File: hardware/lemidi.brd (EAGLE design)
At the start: 76 x 40 mm, 67 parts, among them Q1 IRLML6246, Q2 IRLML6246, Q3 IRLML6246, Q4 IRLML6246, U1 SPX5205 3v3, X1 optional 5V input, X3 debug, Y2 12MHz 0.25%, Y3 8MHz

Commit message: 2nd cleanup
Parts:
- moved U$7 0.72 mm to (72.2, 3.75)
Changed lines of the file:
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@@
 <text x="1.8" y="9.4" size="1.016" layer="1" font="vector" ratio="15" rot="R90">1</text>
 <text x="1.8" y="11.2" size="1.016" layer="16" font="vector" ratio="15" rot="R90">2</text>
-<text x="72.7" y="1.13" size="0.8128" layer="109" font="vector" ratio="15" rot="MR90">github.com/rodan/lemidi</text>
-<text x="74.13" y="1.15" size="0.8128" layer="109" font="vector" ratio="15" rot="MR90">Petre Rodan 201901 rev1</text>
+<text x="71.7" y="7.53" size="0.8128" layer="109" font="vector" ratio="15" rot="MR90">github.com/rodan/lemidi</text>
+<text x="73.13" y="7.55" size="0.8128" layer="109" font="vector" ratio="15" rot="MR90">Petre Rodan 201901 rev1</text>
 <text x="2.23" y="36.83" size="0.8128" layer="109" font="vector" ratio="15" rot="MR270">debug</text>
 <wire x1="1.35" y1="9.35" x2="1.35" y2="12.15" width="1.6764" layer="41"/>
@@
 <element name="C4" library="rcl" package="C0805" value="1uF" x="29.75" y="8.53" rot="R90"/>
 <element name="C6" library="rcl" package="C0805" value="100nF" x="26.55" y="5.43"/>
-<element name="U$7" library="SparkFun" package="OSHW-LOGO-M" value="OSHW-LOGOM" x="71.81" y="4.35" rot="MR90"/>
+<element name="U$7" library="SparkFun" package="OSHW-LOGO-M" value="OSHW-LOGOM" x="72.21" y="3.75" rot="MR90"/>
 <element name="U$1" library="TI_MSP430_v16" package="PT48" value="MSP430F5510" x="28.8" y="28.8"/>
 <element name="C10" library="rcl" package="C0805" value="470nF" x="20.8" y="25" rot="R180"/>

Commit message: 3rd cleanup
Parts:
- removed X1: optional 5V input, Simplex-Connectors:0530480210
- added JP1: external 5v, SparkFun-Connectors:1X02
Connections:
- net 5V_EXT: now also JP1.1; no longer X1.2
- net GND: now also JP1.2; no longer X1.1
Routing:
- net 5V_EXT: track 9.18 -> 8.50 mm
- net GND: vias 35 -> 37
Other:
- board text added: "3V3"
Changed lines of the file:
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@@
 <layer number="97" name="Info" color="7" fill="1" visible="no" active="no"/>
 <layer number="98" name="Guide" color="6" fill="1" visible="no" active="no"/>
+<layer number="99" name="SpiceOrder" color="7" fill="1" visible="no" active="no"/>
 <layer number="100" name="Muster" color="7" fill="1" visible="no" active="no"/>
 <layer number="101" name="Patch_Top" color="12" fill="4" visible="no" active="yes"/>
@@
 <hole x="3.1" y="3.1" drill="3.2"/>
 <rectangle x1="19.7" y1="6.5" x2="21.2" y2="8" layer="30"/>
-<text x="34.73" y="0.97" size="0.8128" layer="109" font="vector" ratio="15" rot="MR0">ext 5V</text>
+<text x="30.47" y="0.77" size="0.8128" layer="108" font="vector" ratio="15">ext 5V</text>
 <text x="1.8" y="9.4" size="1.016" layer="1" font="vector" ratio="15" rot="R90">1</text>
 <text x="1.8" y="11.2" size="1.016" layer="16" font="vector" ratio="15" rot="R90">2</text>
@@
 <wire x1="17.6" y1="29.8" x2="18" y2="29.8" width="0.254" layer="109"/>
 <wire x1="18" y1="29.8" x2="18.8" y2="30.6" width="0.254" layer="109"/>
+<text x="23.27" y="12.57" size="0.8128" layer="108" font="vector" ratio="15">3V3</text>
 </plain>
 <attributes>
@@
 <element name="C3" library="rcl" package="C0805" value="10uF" x="26.55" y="3.33"/>
 <element name="X3" library="Simplex-Connectors" package="0530480610" value="debug" x="4.6" y="38.4" rot="R270"/>
-<element name="X1" library="Simplex-Connectors" package="0530480210" value="optional 5V input" x="32.2" y="4.2"/>
 <element name="R7" library="rcl" package="R0805W" value="4k7" x="16" y="35.4"/>
 <element name="R8" library="rcl" package="R0805W" value="4k7" x="16" y="37.6"/>
@@
 <attribute name="TP_SIGNAL_NAME" value="" x="36.2" y="35.8" size="1.778" layer="28" rot="MR0" display="off"/>
 </element>
+<element name="JP1" library="SparkFun-Connectors" package="1X02" value="external 5v" x="33.8" y="3.4" rot="R180"/>
 </elements>
 <signals>
@@
 <contactref element="C3" pad="2"/>
 <contactref element="X3" pad="6"/>
-<contactref element="X1" pad="1"/>
 <contactref element="Q2" pad="2"/>
 <contactref element="OK1" pad="9"/>
@@
 <via x="1" y="28.2" extent="1-16" drill="0.4"/>
 <via x="1" y="19.4" extent="1-16" drill="0.4"/>
+<via x="29.6" y="11.4" extent="1-16" drill="0.4"/>
+<via x="29.2" y="5.8" extent="1-16" drill="0.4"/>
+<contactref element="JP1" pad="2"/>
 </signal>
 <signal name="+3V3">
@@
 <wire x1="29.2" y1="2.2" x2="29.2" y2="3.8" width="0.6096" layer="1"/>
 <wire x1="43.3" y1="3.2" x2="43.3" y2="2.2" width="0.6096" layer="1"/>
-<wire x1="36.2" y1="3.4" x2="40.6" y2="3.4" width="0.6096" layer="1"/>
 <wire x1="40.6" y1="3.4" x2="41" y2="3.8" width="0.6096" layer="1"/>
 <wire x1="41" y1="3.8" x2="42.8" y2="3.8" width="0.6096" layer="1"/>
@@
 <wire x1="25.6" y1="1.8" x2="28.8" y2="1.8" width="0.6096" layer="1"/>
 <wire x1="28.8" y1="1.8" x2="29.2" y2="2.2" width="0.6096" layer="1"/>
-<wire x1="36.2" y1="3.4" x2="34" y2="5.6" width="0.6096" layer="1"/>
-<wire x1="34" y1="5.6" x2="31" y2="5.6" width="0.6096" layer="1"/>
 <wire x1="31" y1="5.6" x2="29.2" y2="3.8" width="0.6096" layer="1"/>
 <wire x1="5.2" y1="14.6" x2="7" y2="14.6" width="0.6096" layer="1"/>
@@
 <wire x1="44" y1="35.6" x2="44.75" y2="36.35" width="0.4064" layer="1"/>
 <wire x1="44.75" y1="36.35" x2="44.75" y2="37.2" width="0.4064" layer="1"/>
+<wire x1="31" y1="5.6" x2="34.2" y2="5.6" width="0.6096" layer="1"/>
+<wire x1="34.2" y1="5.6" x2="36.4" y2="3.4" width="0.6096" layer="1"/>
+<wire x1="36.4" y1="3.4" x2="40.6" y2="3.4" width="0.6096" layer="1"/>
 </signal>
 <signal name="HIGH_MOSI">
@@
 </signal>
 <signal name="5V_EXT">
-<contactref element="X1" pad="2"/>
 <contactref element="U$11" pad="3"/>
 <wire x1="41.8" y1="2.2" x2="35.45" y2="2.2" width="0.6096" layer="1"/>
-<wire x1="35.45" y1="2.2" x2="33.45" y2="4.2" width="0.6096" layer="1"/>
+<contactref element="JP1" pad="1"/>
+<wire x1="33.8" y1="3.4" x2="34.25" y2="3.4" width="0.6096" layer="1"/>
+<wire x1="34.25" y1="3.4" x2="35.45" y2="2.2" width="0.6096" layer="1"/>
 </signal>
 <signal name="MOSI">

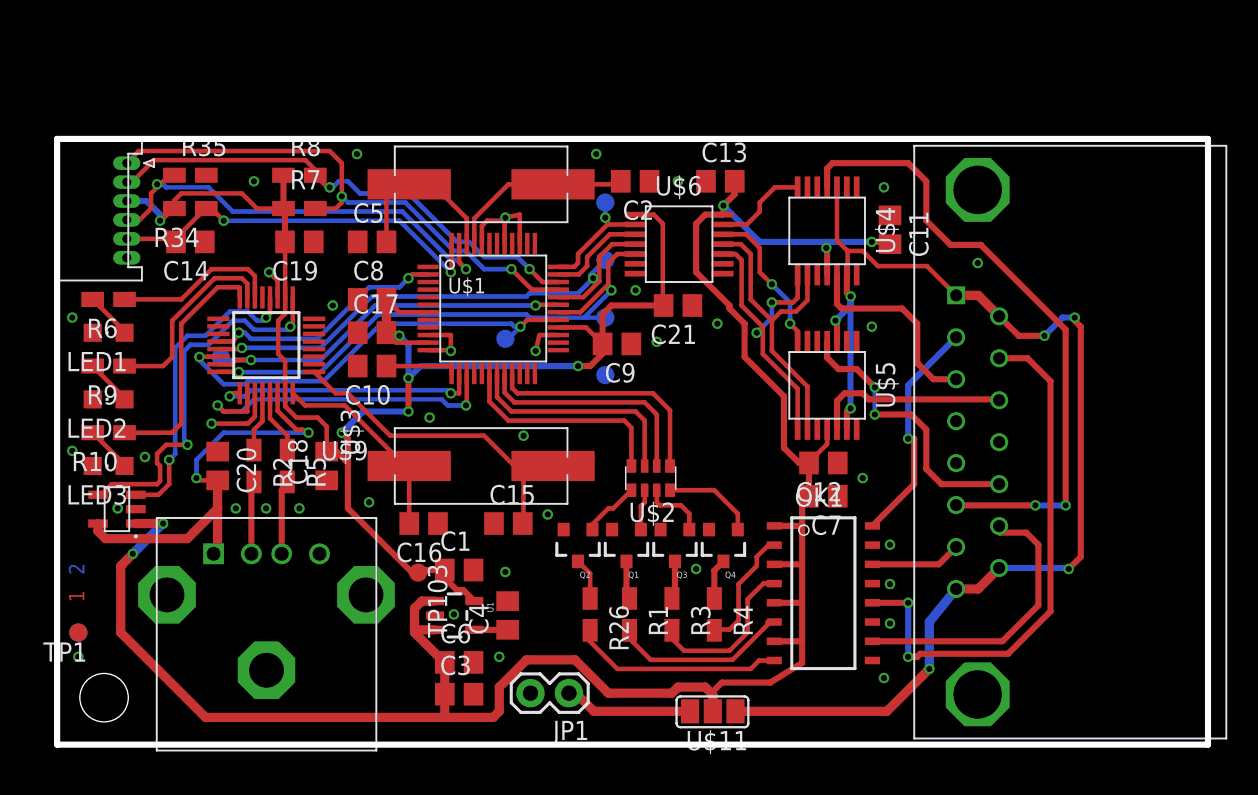
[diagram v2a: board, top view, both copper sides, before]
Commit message: split 5v inputs from the midi connector, add fuse, add reverse polarity protection for external 5v input
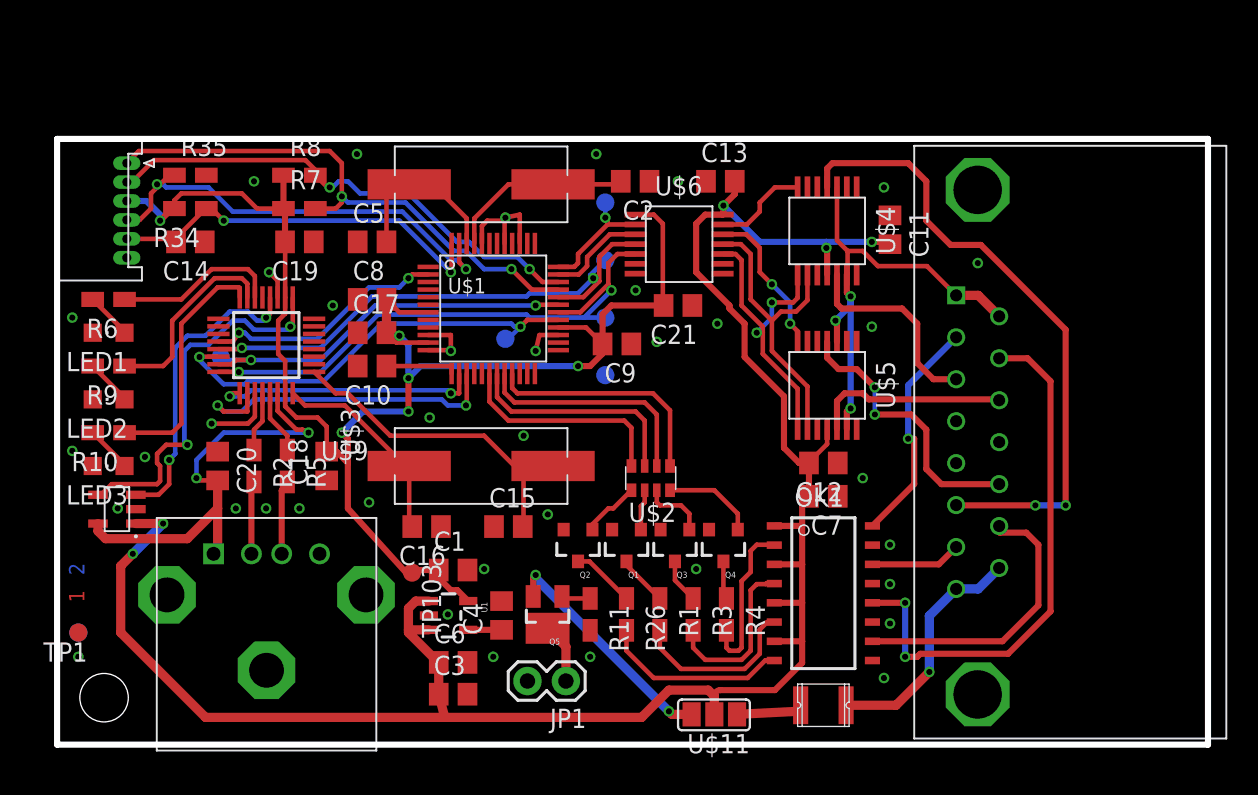
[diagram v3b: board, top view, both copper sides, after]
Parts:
- added Q5: si2305cd, Simplex-DiscreteSemi:SOT23-3_POWER
- added R11: 4k7, rcl:R0805W
- added U$12: RESETTABLE_1210, Simplex-Fuses:1210
- moved R26 2.40 mm to (37.6, 8.60)
- moved R1 2.00 mm to (39.8, 8.60)
- moved R3 1.40 mm to (42.0, 8.60)
- moved JP1 0.82 mm to (33.6, 4.20)
- moved R4 0.80 mm to (44.2, 8.60)
- moved C1 0.40 mm to (26.1, 11.5)
- moved C3 0.40 mm to (26.1, 3.33)
- moved C6 0.40 mm to (26.1, 5.43)
- moved C4 0.40 mm to (29.4, 8.53)
- moved TP103 0.40 mm to (23.4, 11.4)
- moved U1 0.40 mm to (25.9, 8.53)
- moved C16 0.28 mm to (24.4, 14.4)
- moved U$11 0.22 mm to (44.9, 2.00)
- moved C15 0.20 mm to (29.8, 14.4)
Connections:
- new net 5V_PC2: U$10.15, U$10.8, U$12.P$2
- new net N$10: U$11.1, U$12.P$1
- new net N$23: Q5.2, U$11.3
- new net N$24: Q5.1, R11.1
- net 5V_EXT: now also Q5.3; no longer U$11.3
- net 5V_PC: no longer U$10.15, U$10.8, U$11.1
- net GND: now also R11.2
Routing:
- net 5V_PC: track 82.8 -> 31.7 mm, vias 7 -> 3
- net 5V_PC2: track 0.00 -> 16.0 mm, vias 0 -> 1
- net N$23: track 0.00 -> 15.8 mm, vias 0 -> 2
- net 5V_EXT: track 8.50 -> 3.99 mm
- net N$10: track 0.00 -> 4.45 mm
- net +5V: track 137.1 -> 133.6 mm
- net N$15: track 8.05 -> 10.7 mm
- net N$24: track 0.00 -> 1.89 mm
- net N$9: track 14.1 -> 12.4 mm
- net N$22: track 2.78 -> 4.21 mm
- net N$5: track 2.53 -> 3.36 mm
- net N$7: track 12.2 -> 11.5 mm
- net GND: vias 37 -> 38
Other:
- board text added: "+"

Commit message: max5415
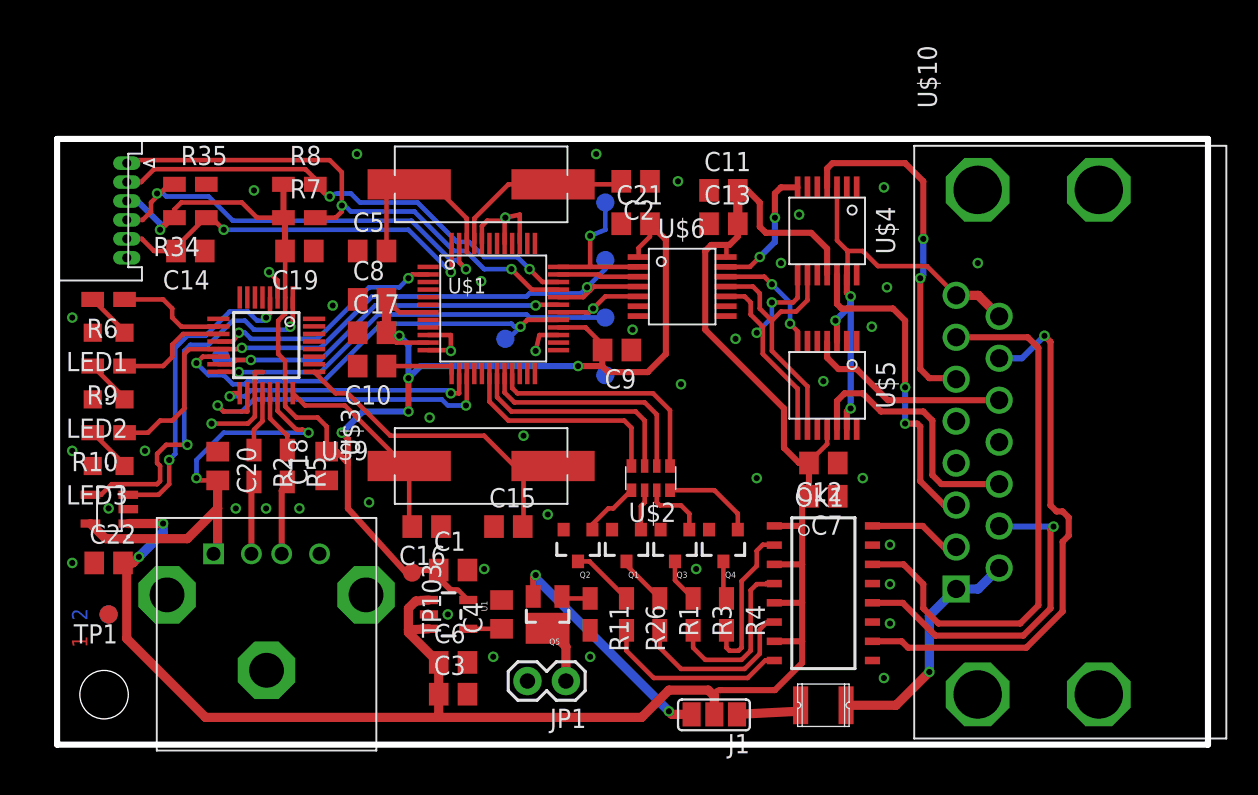
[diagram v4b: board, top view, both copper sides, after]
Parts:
- added C22: 100nF, rcl:C0805
- C18: value 100nF -> 1uF
- C19: value 4.7uF -> 100nF
- C2, C5: value 22pF -> 27pF
- J1: value SJ_3P -> (none)
- R10, R6, R9: value 100k -> 47K
- U$9: value UBA-4R-D14T-4D -> USB-A
- Y2: value 12MHz 0.25% -> 12MHz 0.25% CL 16pF
- Y3: value 8MHz -> 8MHz CL 18pF
- moved C11 11.3 mm to (44.0, 36.6), turned to 0 degrees
- moved C21 6.08 mm to (38.2, 34.4), turned to 0 degrees
- moved C13 2.81 mm to (44.0, 34.4)
- moved U$6 2.81 mm to (38.4, 32.2)
- moved TP1 2.33 mm to (3.40, 8.60)
- moved TP101 2.33 mm to (3.40, 8.60)
- moved U$7 0.89 mm to (73.0, 3.35)
- moved C14 0.60 mm to (8.80, 32.6)
- moved C19 0.60 mm to (16.0, 32.6)
- moved C5 0.60 mm to (20.8, 32.6)
- moved R34 0.60 mm to (8.80, 34.8)
- moved R35 0.60 mm to (8.80, 37.0)
- moved R7 0.60 mm to (16.0, 34.8)
- moved R8 0.60 mm to (16.0, 37.0)
- moved U$8 0.50 mm to (4.70, 14.6)
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- renumbered U$11 to J1
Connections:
- net TP5 renamed CS_J1
- removed net USB_ST1: R9.1, U$3.7
- removed net USB_ST2: R10.1, U$3.8
- removed net USB_ST3: R6.1, U$3.6
- new net STATUS1: R6.1, U$3.10
- new net STATUS2: R9.1, U$3.11
- net +5V: now also C22.2
- net 5V_PC: now also U$10.15, U$10.8; no longer U$10.1, U$10.9
- net 5V_PC2: now also U$10.1, U$10.9; no longer U$10.15, U$10.8
- net GND: now also C22.1, U$10.SH@3, U$10.SH@4
- net SCLK: now also R10.1
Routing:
- net B2: track 6.00 -> 36.7 mm
- net J1Y: track 42.1 -> 23.4 mm
- net B4: track 19.3 -> 36.6 mm, vias 0 -> 1
- net USB_ST2: track 16.1 -> 0.00 mm
- net B3: track 35.8 -> 22.5 mm, vias 2 -> 1
- net USB_ST1: track 13.0 -> 0.00 mm
- net USB_ST3: track 11.0 -> 0.00 mm
- net B1: track 15.3 -> 6.15 mm, vias 1 -> 0
- net SCLK: track 36.4 -> 44.8 mm
- net J1X: track 13.4 -> 21.4 mm, vias 0 -> 2
- net STATUS2: track 0.00 -> 7.54 mm
- net STATUS1: track 0.00 -> 7.30 mm
- net J2Y: track 18.4 -> 13.6 mm, vias 2 -> 0
- net J2X: track 13.0 -> 17.4 mm
- net MOSI: track 37.9 -> 33.8 mm
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
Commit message: switch to MCP42xxx digital pot
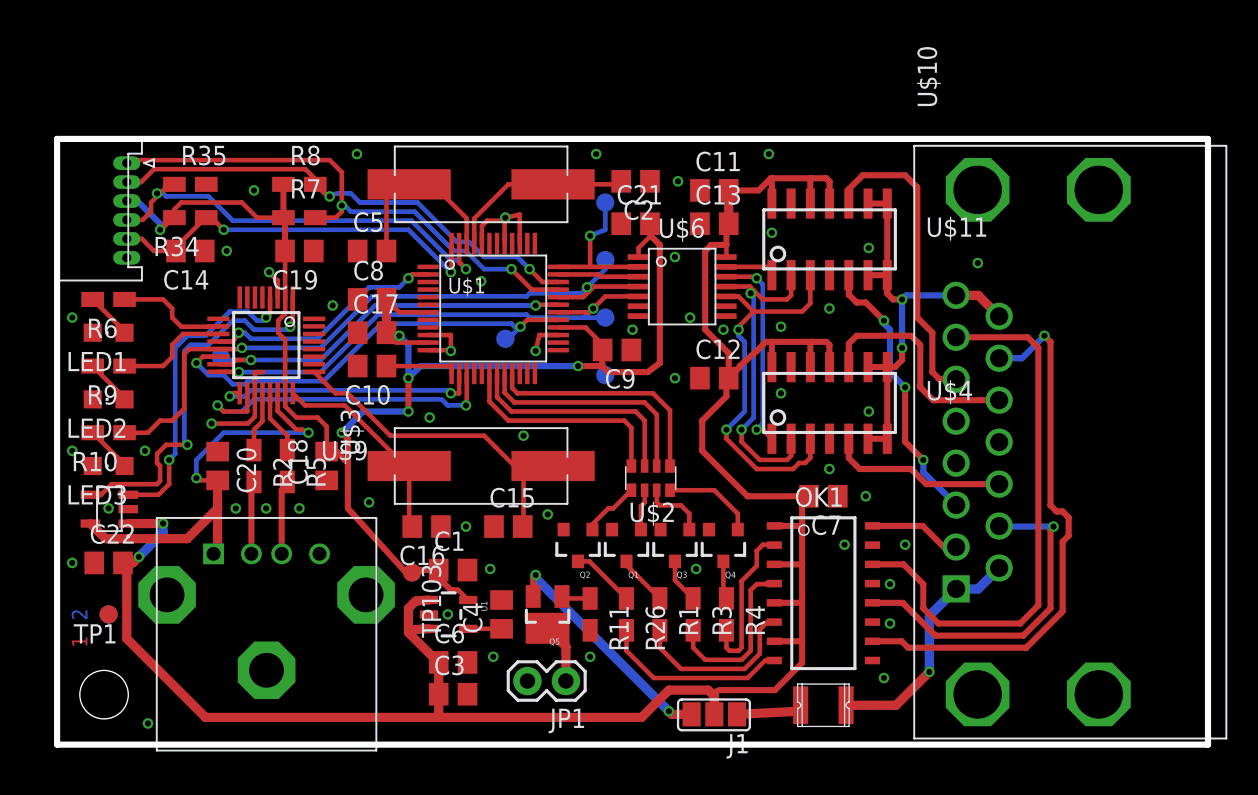
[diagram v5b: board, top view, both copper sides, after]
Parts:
- removed U$5: MAX5413, Simplex-ICs:TSSOP14
- added U$11: MCP42XX, Simplex-ICs:SO-14
- U$4: value MAX5413 -> MCP42XX; device Simplex-ICs:TSSOP14 -> Simplex-ICs:SO-14
- moved U$4 17.5 mm to (47.2, 20.2), turned to 0 degrees
- moved C12 9.12 mm to (43.4, 24.2), turned to 0 degrees
- moved C11 0.60 mm to (43.4, 36.6)
- moved C13 0.60 mm to (43.4, 34.4)
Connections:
- net +5V: now also U$11.11, U$11.12, U$11.14, U$4.12, U$4.14; no longer U$5.11
- net 5V_PC: now also U$11.6, U$11.7, U$11.8, U$11.9, U$4.6, U$4.7, U$4.8, U$4.9; no longer U$4.13, U$4.3, U$5.13, U$5.3
- net GND: now also U$11.4, U$4.4; no longer U$4.1, U$5.1
- net HIGH_CS1: now also U$11.1; no longer U$4.7
- net HIGH_CS2: now also U$4.1; no longer U$5.7
- net HIGH_MOSI: now also U$11.3, U$4.3; no longer U$4.8, U$5.8
- net HIGH_SCLK: now also U$11.2, U$4.2; no longer U$4.9, U$5.9
- net J1X: now also U$11.5; no longer U$4.12
- net J1Y: now also U$11.10; no longer U$4.4
- net J2X: now also U$4.5; no longer U$5.12
- net J2Y: now also U$4.10; no longer U$5.4
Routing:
- net +5V: track 130.2 -> 144.7 mm
- net HIGH_MOSI: track 17.6 -> 25.5 mm
- net HIGH_CS2: track 7.76 -> 13.7 mm
- net J2X: track 17.4 -> 11.9 mm
- net HIGH_CS1: track 8.80 -> 3.60 mm, vias 2 -> 0
- net HIGH_SCLK: track 17.3 -> 21.6 mm, vias 0 -> 2
- net J1X: track 21.4 -> 18.5 mm, vias 2 -> 3
- net J1Y: track 23.4 -> 20.6 mm, vias 2 -> 0
- net 5V_PC: track 31.7 -> 29.2 mm, vias 3 -> 2
- net J2Y: track 13.6 -> 15.1 mm
- net GND: vias 44 -> 51

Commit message: latest
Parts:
- U$11, U$4: value MCP42XX -> MCP42100
- moved C12 1.60 mm to (43.4, 25.8)
- moved C9 0.26 mm to (37.0, 25.8)
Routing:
- net +3V3: track 104.4 -> 105.4 mm
- net J1Y: track 20.6 -> 19.8 mm
- net +5V: track 144.7 -> 144.0 mm
